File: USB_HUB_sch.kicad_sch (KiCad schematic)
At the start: 1 part, among them IC1 USB2513B_M2

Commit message: Updata the USB Hub Sheet
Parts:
- added C1, C2: 18pF, C0402C104K4RAC:CAPC1005X55N, symbol C0402C104K4RAC:C0402C104K4RAC
- added C10: 4.7uF, C0402C104K4RAC:CAPC1005X55N, symbol C0402C104K4RAC:C0402C104K4RAC
- added C11, C12, C13, C14, C3, C4, C5, C6, C7, C8, C9: 0.1uF, C0402C104K4RAC:CAPC1005X55N, symbol C0402C104K4RAC:C0402C104K4RAC
- added R10, R5, R7, R8, R9: 100K, Resistor_SMD:R_0402_1005Metric, symbol Device:R_Small_US
- added R6: 12K, Resistor_SMD:R_0402_1005Metric, symbol Device:R_Small_US
- added Y1: MURATA_XRCGB24M000FFS1DR0, Crystal:MURATA_XRCGB24M000FFS1DR0_0, symbol MURATA_XRCGB24M000FFS1DR0:MURATA_XRCGB24M000FFS1DR0
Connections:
- net STM_D_N: now reaches IC1.1 (USBDM_DN1/PRT_DIS_M1)
- net +3.3V: now reaches IC1.10 (VDDA33_2)
- net +3.3V: now also IC1.15 (VDD33_1), IC1.23 (VDD33_2), IC1.29 (VDDA33_3), IC1.36 (VDDA33_4), IC1.5 (VDDA33_1), C10.2, C4.2, C5.2, C6.2, C7.2, C8.2, C9.2, R5.2
- net GND: now reaches IC1.11 (TEST)
- net GND: now also IC1.37 (GND), C1.2, C10.1, C11.1, C12.1, C13.1, C14.1, C2.2, C3.1, C4.1, C5.1, C6.1, C7.1, C8.1, C9.1, R10.2, R6.1, R7.2, R8.2, R9.1
- net CR: now reaches IC1.14 (CRFILT)
- net CR: now also C13.2, C14.2
- net STM_D_P: now reaches IC1.2 (USBDP_DN1/PRT_DIS_P1)
- net at IC1.22 (SDA/SMBDATA/NON_REM1): now also R10.1
- net at IC1.24 (SCL/SMBCLK/CFG_SEL0): now also R8.1
- net at IC1.25 (HS_IND/CFG_SEL1): now also R7.1
- net at IC1.26 (RESET_N): now also C3.2, R5.1
- net VBUS: now reaches IC1.27 (VBUS_DET)
- net at IC1.28 (SUSP_IND/LOCAL_PWR/NON_REM0): now also R9.2
- net ESP_D_N: now reaches IC1.3 (USBDM_DN2/PRT_DIS_M2)
- net USB_U_N: now reaches IC1.30 (USBDM_UP)
- net USB_U_P: now reaches IC1.31 (USBDP_UP)
- net at IC1.32 (XTALOUT): now also C2.1, Y1.1
- net at IC1.33 (XTALIN/CLKIN): now also C1.1, Y1.3
- net PLL: now reaches IC1.34 (PLLFILT)
- net PLL: now also C11.2, C12.2
- net at IC1.35 (RBIAS): now also R6.2
- net ESP_D_P: now reaches IC1.4 (USBDP_DN2/PRT_DIS_P2)
- net GNSS_D_N: now reaches IC1.6 (USBDM_DN3/PRT_DIS_M3)
- net GNSS_D_P: now reaches IC1.7 (USBDP_DN3/PRT_DIS_P3)
- no-connect marks 0 -> 12
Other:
- note added: "DE-CAPS"
- moved on the sheet: IC1

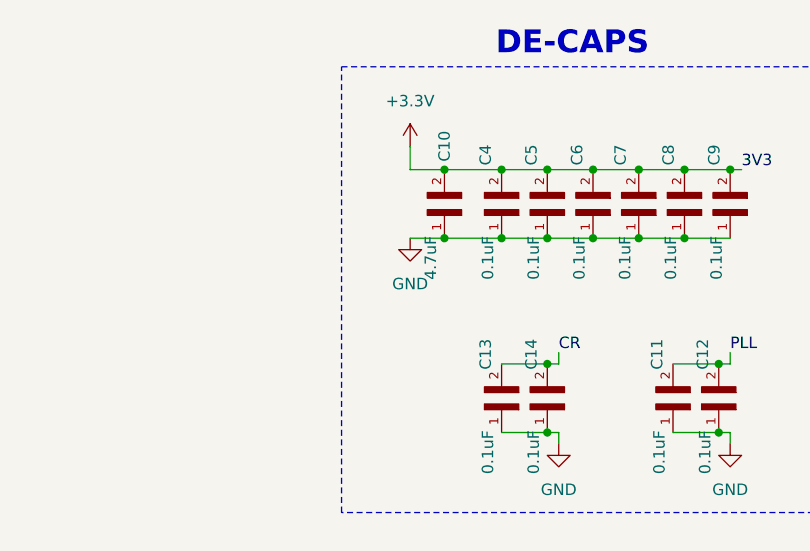
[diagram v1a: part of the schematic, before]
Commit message: update the power sheet
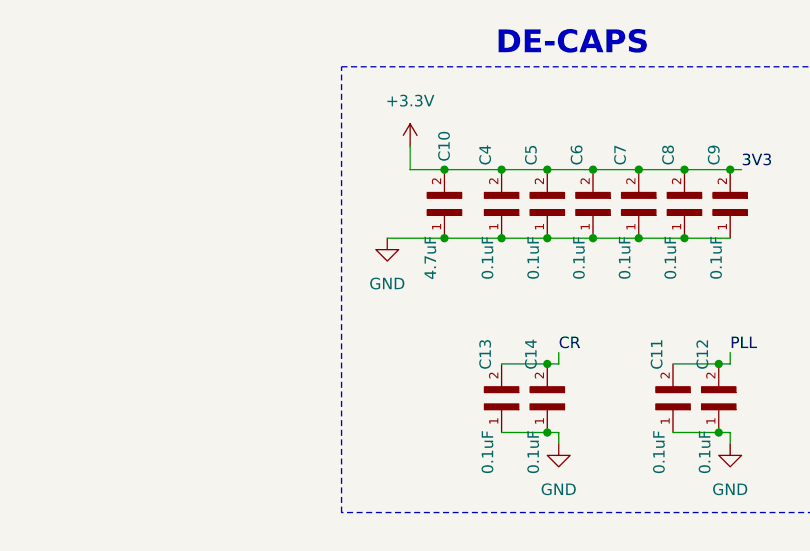
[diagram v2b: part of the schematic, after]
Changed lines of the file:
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@@
 	(wire
 		(pts
-			(xy 213.36 50.8) (xy 217.17 50.8)
+			(xy 210.82 50.8) (xy 217.17 50.8)
 		)
 		(stroke
@@
 	(symbol
 		(lib_id "power:GND")
-		(at 213.36 50.8 0)
+		(at 210.82 50.8 0)
 		(unit 1)
 		(exclude_from_sim no)
@@
 		(fields_autoplaced yes)
 		(property "Reference" "#PWR019"
-			(at 213.36 57.15 0)
+			(at 210.82 57.15 0)
 			(effects
 				(font
@@
 		)
 		(property "Value" "GND"
-			(at 213.36 55.88 0)
+			(at 210.82 55.88 0)
 			(effects
 				(font
@@
 		)
 		(property "Footprint" ""
-			(at 213.36 50.8 0)
+			(at 210.82 50.8 0)
 			(effects
 				(font
@@
 		)
 		(property "Datasheet" ""
-			(at 213.36 50.8 0)
+			(at 210.82 50.8 0)
 			(effects
 				(font
@@
 		)
 		(property "Description" "Power symbol creates a global label with name \"GND\" , ground"
-			(at 213.36 50.8 0)
+			(at 210.82 50.8 0)
 			(effects
 				(font

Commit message: new
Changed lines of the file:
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@@
-		)
-	)
-	(label "GNSS_D_N"
-		(at 148.59 149.86 270)
-		(effects
-			(font
-				(size 1.27 1.27)
-				(color 18 255 0 1)
-			)
-			(justify right bottom)
 		)
 	)
@@
 		)
 	)
-	(label "ESP_D_P"
-		(at 143.51 149.86 270)
-		(effects
-			(font
-				(size 1.27 1.27)
-				(color 18 255 0 1)
-			)
-			(justify right bottom)
-		)
-	)
-	(label "GNSS_D_P"
-		(at 151.13 149.86 270)
-		(effects
-			(font
-				(size 1.27 1.27)
-				(color 18 255 0 1)
-			)
-			(justify right bottom)
-		)
-	)
 	(label "USB_U_P"
 		(at 90.17 111.76 180)
@@
 		)
 	)
-	(label "ESP_D_N"
-		(at 140.97 149.86 270)
-		(effects
-			(font
-				(size 1.27 1.27)
-				(color 18 255 0 1)
-			)
-			(justify right bottom)
-		)
-	)
 	(label "CR"
 		(at 229.87 63.5 0)
@@
 		)
 	)
-	(label "STM_D_P"
-		(at 138.43 149.86 270)
-		(effects
-			(font
-				(size 1.27 1.27)
-				(color 18 255 0 1)
-			)
-			(justify right bottom)
-		)
-	)
 	(label "3V3"
 		(at 184.15 114.3 0)
@@
 		)
 	)
-	(label "STM_D_N"
-		(at 135.89 149.86 270)
+	(global_label "GNSS_D_P"
+		(shape input)
+		(at 151.13 149.86 270)
+		(fields_autoplaced yes)
 		(effects
 			(font
 				(size 1.27 1.27)
-				(color 18 255 0 1)
-			)
-			(justify right bottom)
+				(color 0 0 0 1)
+			)
+			(justify right)
+		)
+		(property "Intersheetrefs" "${INTERSHEET_REFS}"
+			(at 151.13 162.3399 90)
+			(effects
+				(font
+					(size 1.27 1.27)
+				)
+				(justify right)
+				(hide yes)
+			)
+		)
+	)
+	(global_label "ESP_D_P"
+		(shape input)
+		(at 143.51 149.86 270)
+		(fields_autoplaced yes)
+		(effects
+			(font
+				(size 1.27 1.27)
+				(color 0 0 0 1)
+			)
+			(justify right)
+		)
+		(property "Intersheetrefs" "${INTERSHEET_REFS}"
+			(at 143.51 160.9489 90)
+			(effects
+				(font
+					(size 1.27 1.27)
+				)
+				(justify right)
+				(hide yes)
+			)
+		)
+	)
+	(global_label "ESP_D_N"
+		(shape input)
+		(at 140.97 149.86 270)
+		(fields_autoplaced yes)
+		(effects
+			(font
+				(size 1.27 1.27)
+				(color 0 0 0 1)
+			)
+			(justify right)
+		)
+		(property "Intersheetrefs" "${INTERSHEET_REFS}"
+			(at 140.97 161.0094 90)
+			(effects
+				(font
+					(size 1.27 1.27)
+				)
+				(justify right)
+				(hide yes)
+			)
+		)
+	)
+	(global_label "GNSS_D_N"
+		(shape input)
+		(at 148.59 149.86 270)
+		(fields_autoplaced yes)
+		(effects
+			(font
+				(size 1.27 1.27)
+				(color 0 0 0 1)
+			)
+			(justify right)
+		)
+		(property "Intersheetrefs" "${INTERSHEET_REFS}"
+			(at 148.59 162.4004 90)
+			(effects
+				(font
+					(size 1.27 1.27)
+				)
+				(justify right)
+				(hide yes)
+			)
+		)
+	)
+	(global_label "STM_D_P"
+		(shape input)
+		(at 138.43 149.86 270)
+		(fields_autoplaced yes)
+		(effects
+			(font
+				(size 1.27 1.27)
+				(color 0 0 0 1)
+			)
+			(justify right)
+		)
+		(property "Intersheetrefs" "${INTERSHEET_REFS}"
+			(at 138.43 160.9489 90)
+			(effects
+				(font
+					(size 1.27 1.27)
+				)
+				(justify right)
+				(hide yes)
+			)
+		)
+	)
+	(global_label "STM_D_N"
+		(shape input)
+		(at 135.89 149.86 270)
+		(fields_autoplaced yes)
+		(effects
+			(font
+				(size 1.27 1.27)
+				(color 0 0 0 1)
+			)
+			(justify right)
+		)
+		(property "Intersheetrefs" "${INTERSHEET_REFS}"
+			(at 135.89 161.0094 90)
+			(effects
+				(font
+					(size 1.27 1.27)
+				)
+				(justify right)
+				(hide yes)
+			)
 		)
 	)
@@
 		)
 		(property "Value" "+3.3V"
-			(at 145.542 156.718 90)
-			(effects
-				(font
+			(at 146.05 157.48 90)
+			(effects
+				(font

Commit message: New
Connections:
- net USB_U_N renamed DN
- net USB_U_P renamed DP
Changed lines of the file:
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@@
 	)
 	(junction
-		(at 228.6 64.77)
+		(at 228.6 59.69)
 		(diameter 0)
 		(color 0 0 0 0)
@@
 	(wire
 		(pts
-			(xy 229.87 63.5) (xy 229.87 64.77)
-		)
-		(stroke
-			(width 0)
-			(type default)
-		)
-	)
-	(wire
-		(pts
-			(xy 223.52 64.77) (xy 228.6 64.77)
+			(xy 223.52 59.69) (xy 228.6 59.69)
 		)
 		(stroke
@@
 	(wire
 		(pts
+			(xy 223.52 59.69) (xy 223.52 64.77)
+		)
+		(stroke
+			(width 0)
+			(type default)
+		)
+	)
+	(wire
+		(pts
 			(xy 223.52 43.18) (xy 228.6 43.18)
 		)
@@
 	(wire
 		(pts
+			(xy 228.6 59.69) (xy 228.6 64.77)
+		)
+		(stroke
+			(width 0)
+			(type default)
+		)
+	)
+	(wire
+		(pts
 			(xy 242.57 72.39) (xy 247.65 72.39)
 		)
@@
 	(wire
 		(pts
-			(xy 228.6 64.77) (xy 229.87 64.77)
+			(xy 228.6 59.69) (xy 231.14 59.69)
 		)
 		(stroke
@@
 		)
 	)
-	(label "USB_U_N"
-		(at 90.17 109.22 180)
-		(fields_autoplaced yes)
-		(effects
-			(font
-				(size 1.27 1.27)
-				(color 255 12 19 1)
-			)
-			(justify right bottom)
-		)
-	)
 	(label "3V3"
 		(at 184.15 127 0)
@@
 		)
 	)
-	(label "USB_U_P"
-		(at 90.17 111.76 180)
-		(fields_autoplaced yes)
-		(effects
-			(font
-				(size 1.27 1.27)
-				(color 255 22 18 1)
-			)
-			(justify right bottom)
-		)
-	)
 	(label "CR"
-		(at 229.87 63.5 0)
+		(at 231.14 59.69 0)
 		(fields_autoplaced yes)
 		(effects
@@
 			)
 			(justify left bottom)
+		)
+	)
+	(global_label "DP"
+		(shape input)
+		(at 90.17 111.76 180)
+		(fields_autoplaced yes)
+		(effects
+			(font
+				(size 1.27 1.27)
+			)
+			(justify right)
+		)
+		(property "Intersheetrefs" "${INTERSHEET_REFS}"
+			(at 84.6448 111.76 0)
+			(effects
+				(font
+					(size 1.27 1.27)
+				)
+				(justify right)
+				(hide yes)
+			)
 		)
 	)
@@
 			(effects
 				(font
+					(size 1.27 1.27)
+				)
+				(justify right)
+				(hide yes)
+			)
+		)
+	)
+	(global_label "DN"
+		(shape input)
+		(at 90.17 109.22 180)
+		(fields_autoplaced yes)
+		(effects
+			(font
+				(size 1.27 1.27)
+			)
+			(justify right)
+		)
+		(property "Intersheetrefs" "${INTERSHEET_REFS}"
+			(at 84.5843 109.22 0)
+			(effects
+				(font

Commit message: new can
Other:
- note added: "USB_HUB"
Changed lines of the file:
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@@
+		)
+	)
+	(text "USB_HUB"
+		(exclude_from_sim no)
+		(at 45.974 46.228 0)
+		(effects
+			(font
+				(size 2.54 2.54)
+				(bold yes)
+			)
 		)
 	)

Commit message: schamtic Update
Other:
- moved on the sheet: C10, C11, C12, C13, C14, C4, C5, C6, C7, C8, C9
